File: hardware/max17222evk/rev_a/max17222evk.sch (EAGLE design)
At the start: 30 parts, among them U1 MAX17222, U2 MAX17222

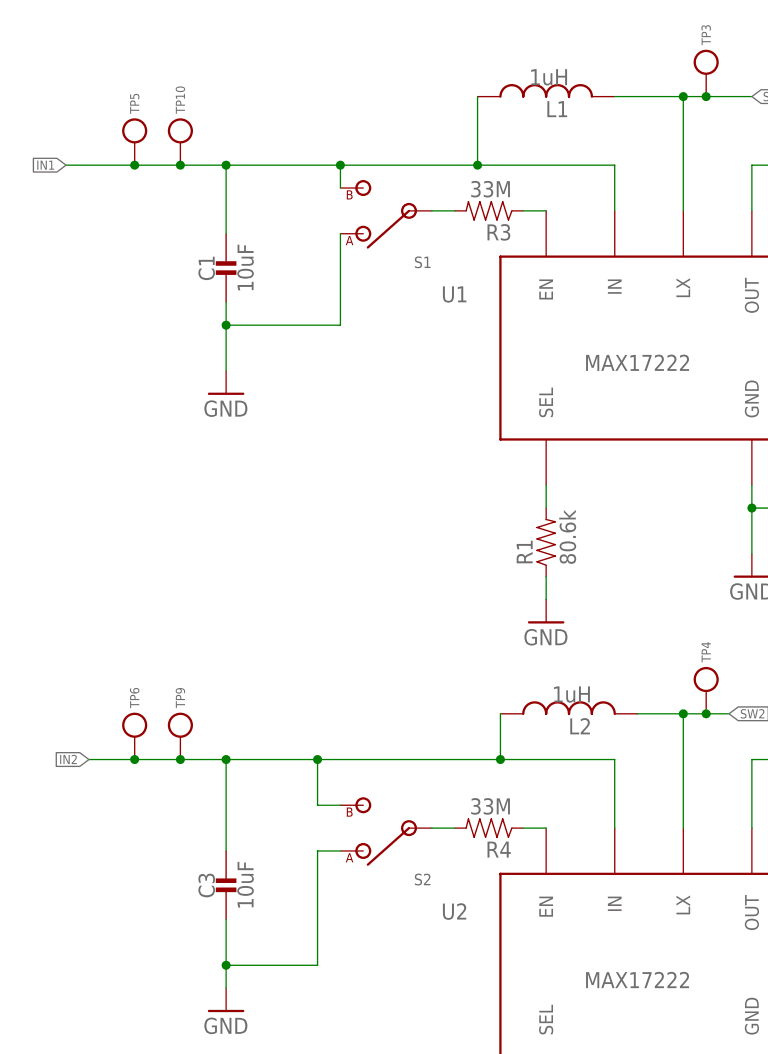
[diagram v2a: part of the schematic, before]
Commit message: added mounting holes, fixed switch
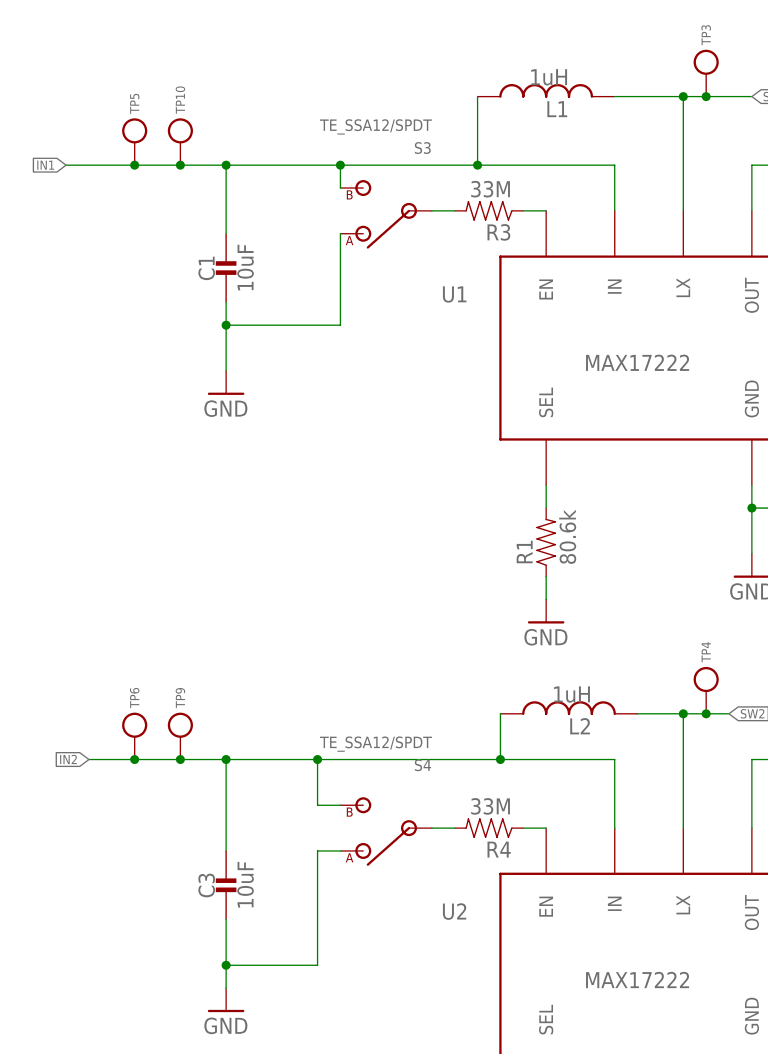
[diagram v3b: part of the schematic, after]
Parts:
- removed S1, S2: CL-SB-12X, switches:CL-SB-12X
- added S3, S4: TE_SSA12/SPDT, switches:TE_SSA12/SPDT
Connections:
- net GND: now also S3.A, S4.A; no longer S1.1, S2.1
- net IN1: now also S3.B; no longer S1.3
- net IN2: now also S4.B; no longer S2.3
- net N$1: now also S3.IN; no longer S1.2
- net N$3: now also S4.IN; no longer S2.2
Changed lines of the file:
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@@
 <part name="L1" library="passives" deviceset="INDUCTOR" device="IHL2525CZ" value="1uH"/>
 <part name="L2" library="passives" deviceset="INDUCTOR" device="DFE322512C" value="1uH"/>
-<part name="S1" library="switches" deviceset="CL-SB-12X" device=""/>
-<part name="S2" library="switches" deviceset="CL-SB-12X" device=""/>
 <part name="GND5" library="supply1" library_urn="urn:adsk.eagle:library:371" deviceset="GND" device=""/>
 <part name="GND6" library="supply1" library_urn="urn:adsk.eagle:library:371" deviceset="GND" device=""/>
@@
 <part name="R3" library="passives" deviceset="RESISTOR" device="0603_RES" value="33M"/>
 <part name="R4" library="passives" deviceset="RESISTOR" device="0603_RES" value="33M"/>
+<part name="S3" library="switches" deviceset="TE_SSA12/SPDT" device=""/>
+<part name="S4" library="switches" deviceset="TE_SSA12/SPDT" device=""/>
 </parts>
 <sheets>
@@
 <instance part="L1" gate="G$1" x="109.22" y="165.1" rot="R90"/>
 <instance part="L2" gate="G$1" x="111.76" y="96.52" rot="R90"/>
-<instance part="S1" gate="G$1" x="93.98" y="152.4" rot="R180"/>
-<instance part="S2" gate="G$1" x="93.98" y="83.82" rot="R180"/>
 <instance part="GND5" gate="1" x="73.66" y="132.08"/>
 <instance part="GND6" gate="1" x="73.66" y="63.5"/>
@@
 <instance part="R3" gate="G$1" x="101.6" y="152.4" rot="R180"/>
 <instance part="R4" gate="G$1" x="101.6" y="83.82" rot="R180"/>
+<instance part="S3" gate="G$1" x="93.98" y="152.4" rot="R180"/>
+<instance part="S4" gate="G$1" x="93.98" y="83.82" rot="R180"/>
 </instances>
 <busses>
@@
 <wire x1="73.66" y1="149.86" x2="73.66" y2="157.48" width="0.1524" layer="91"/>
 <junction x="73.66" y="157.48"/>
-<pinref part="S1" gate="G$1" pin="3"/>
 <wire x1="86.36" y1="154.94" x2="86.36" y2="157.48" width="0.1524" layer="91"/>
 <junction x="86.36" y="157.48"/>
@@
 <pinref part="TP10" gate="G$1" pin="TESTPOINT"/>
 <junction x="68.58" y="157.48"/>
+<pinref part="S3" gate="G$1" pin="B"/>
 </segment>
 </net>
@@
 <pinref part="C1" gate="G$1" pin="2"/>
 <wire x1="73.66" y1="134.62" x2="73.66" y2="139.7" width="0.1524" layer="91"/>
-<pinref part="S1" gate="G$1" pin="1"/>
 <wire x1="73.66" y1="139.7" x2="73.66" y2="142.24" width="0.1524" layer="91"/>
 <wire x1="86.36" y1="149.86" x2="86.36" y2="139.7" width="0.1524" layer="91"/>
 <wire x1="86.36" y1="139.7" x2="73.66" y2="139.7" width="0.1524" layer="91"/>
 <junction x="73.66" y="139.7"/>
+<pinref part="S3" gate="G$1" pin="A"/>
 </segment>
 <segment>
@@
 </segment>
 <segment>
-<pinref part="S2" gate="G$1" pin="1"/>
 <wire x1="86.36" y1="81.28" x2="83.82" y2="81.28" width="0.1524" layer="91"/>
 <wire x1="83.82" y1="81.28" x2="83.82" y2="68.58" width="0.1524" layer="91"/>
@@
 <wire x1="73.66" y1="68.58" x2="73.66" y2="73.66" width="0.1524" layer="91"/>
 <junction x="73.66" y="68.58"/>
+<pinref part="S4" gate="G$1" pin="A"/>
 </segment>
 <segment>
@@
 <wire x1="116.84" y1="83.82" x2="116.84" y2="91.44" width="0.1524" layer="91"/>
 <wire x1="116.84" y1="91.44" x2="104.14" y2="91.44" width="0.1524" layer="91"/>
-<pinref part="S2" gate="G$1" pin="3"/>
 <wire x1="104.14" y1="91.44" x2="83.82" y2="91.44" width="0.1524" layer="91"/>
 <wire x1="83.82" y1="91.44" x2="73.66" y2="91.44" width="0.1524" layer="91"/>
@@
 <pinref part="TP9" gate="G$1" pin="TESTPOINT"/>
 <junction x="68.58" y="91.44"/>
+<pinref part="S4" gate="G$1" pin="B"/>
 </segment>
 </net>
@@
 <net name="N$1" class="0">
 <segment>
-<pinref part="S1" gate="G$1" pin="2"/>
 <pinref part="R3" gate="G$1" pin="2"/>
 <wire x1="96.52" y1="152.4" x2="99.06" y2="152.4" width="0.1524" layer="91"/>
+<pinref part="S3" gate="G$1" pin="IN"/>
 </segment>
 </net>
@@
 <net name="N$3" class="0">
 <segment>
-<pinref part="S2" gate="G$1" pin="2"/>
 <pinref part="R4" gate="G$1" pin="2"/>
 <wire x1="96.52" y1="83.82" x2="99.06" y2="83.82" width="0.1524" layer="91"/>
-</segment>
-</net>
+<pinref part="S4" gate="G$1" pin="IN"/>
+</segment>
+</net>

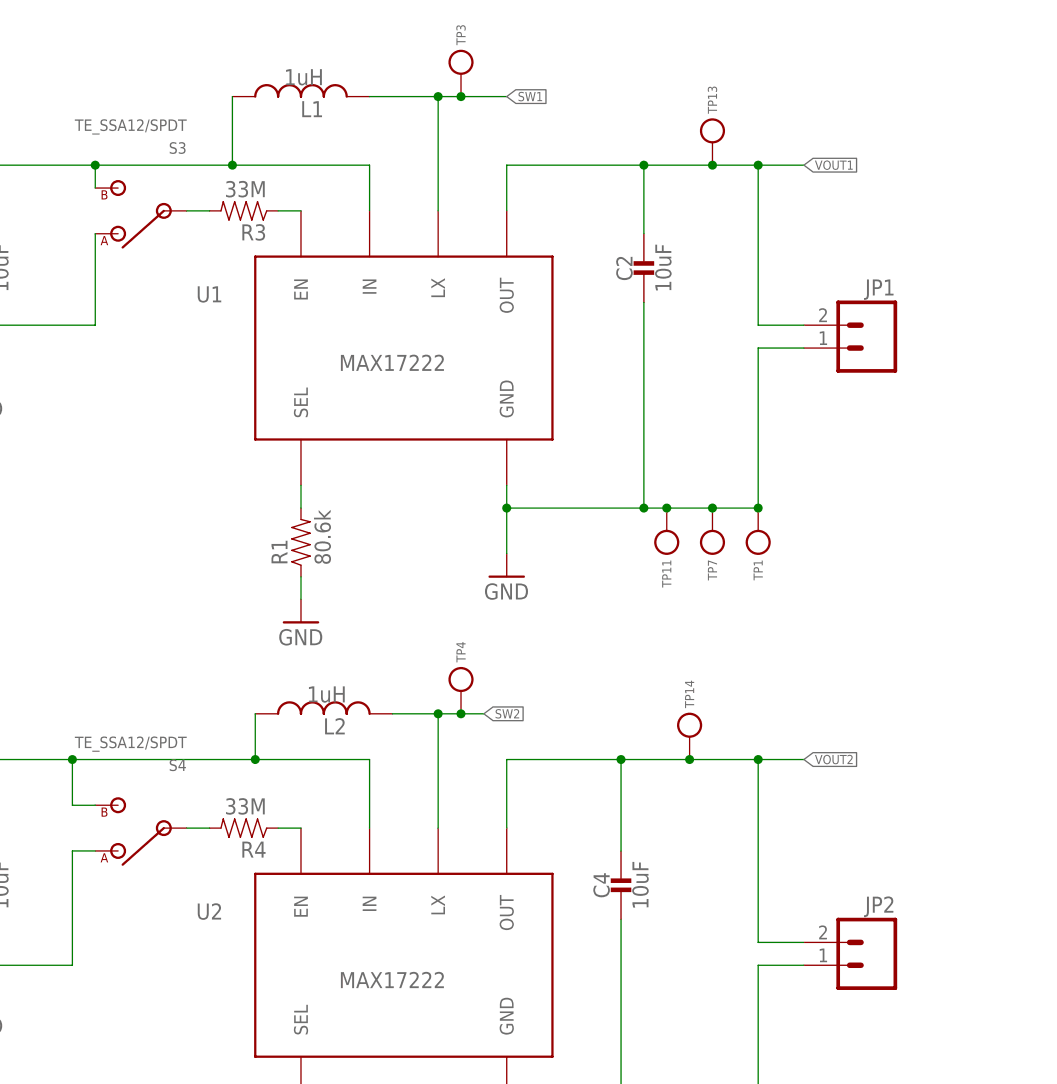
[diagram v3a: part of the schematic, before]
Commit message: added part numbers and associated BOM
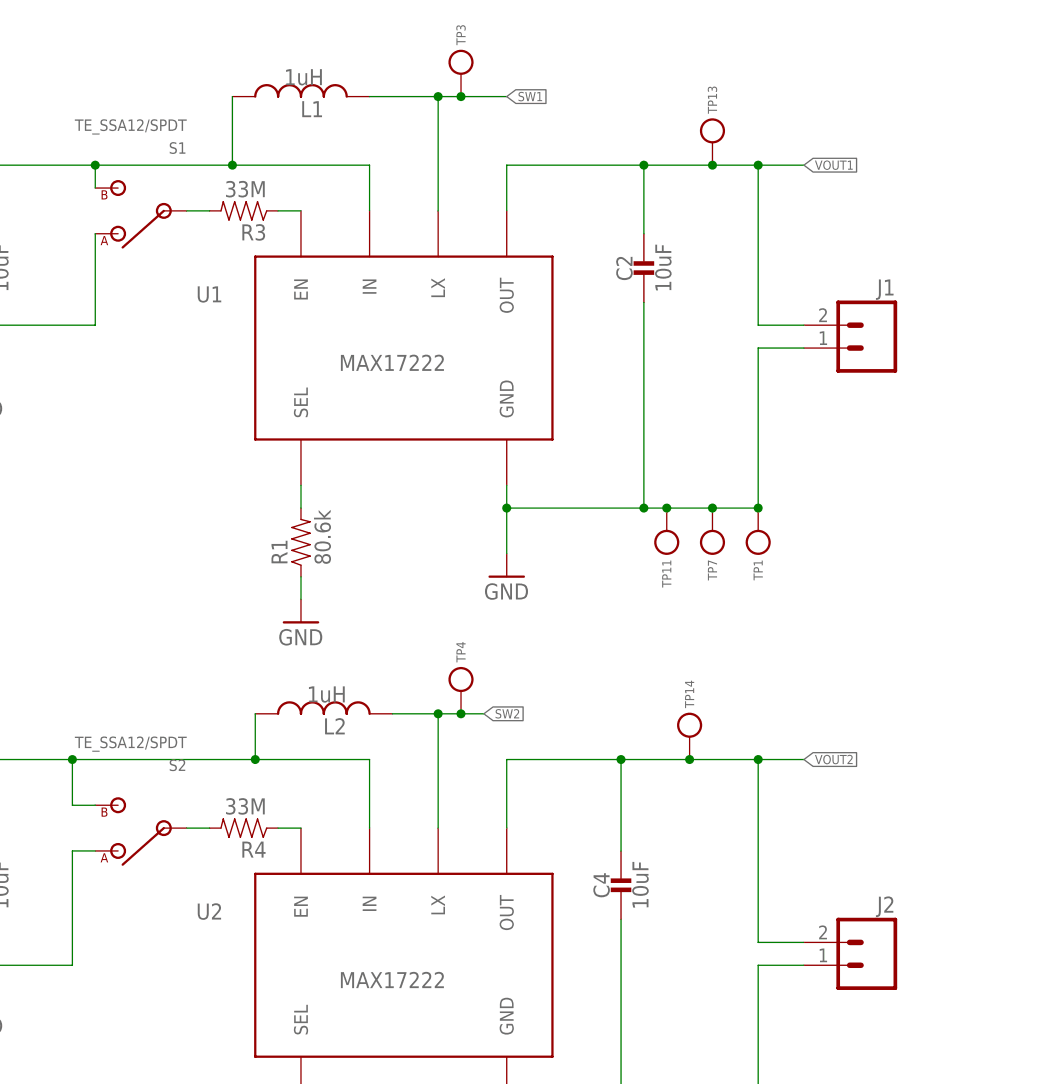
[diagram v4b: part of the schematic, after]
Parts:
- C1, C2, C3, C4: DIGIKEY (none) -> 490-3896-2-ND
- J1, J2: DIGIKEY (none) -> 277-1721-ND
- L1: DIGIKEY (none) -> 541-2562-1-ND
- L2: DIGIKEY (none) -> 490-10590-1-ND
- R1, R2: DIGIKEY (none) -> 311-80.6KHRCT-ND
- R3, R4: DIGIKEY (none) -> HMC0603JT33M0CT-ND
- TP1, TP11, TP12, TP2: DIGIKEY (none) -> 36-1519-2-ND
- renumbered JP1 to J1, JP2 to J2, S3 to S1, S4 to S2
